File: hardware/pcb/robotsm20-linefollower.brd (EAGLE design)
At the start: 230 x 100 mm, 139 parts, among them Q5 BSS138LT3G, Q6 BSS138LT3G, Q7 BSS138LT3G, Q8 BSS138LT3G, SW1 CTS_219-4LPST, U1 STM32F405RG

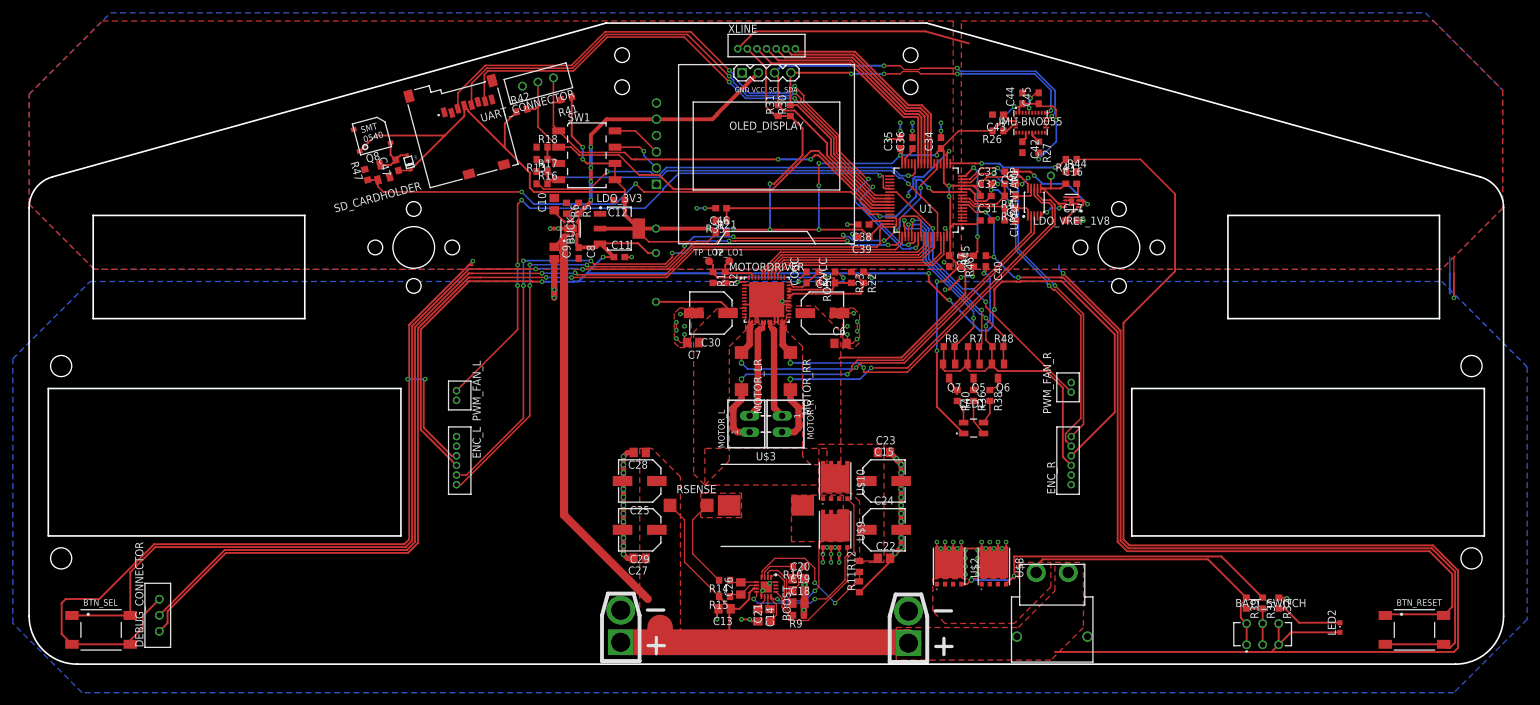
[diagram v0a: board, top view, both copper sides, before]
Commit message: Added more text and continue the DRC fun
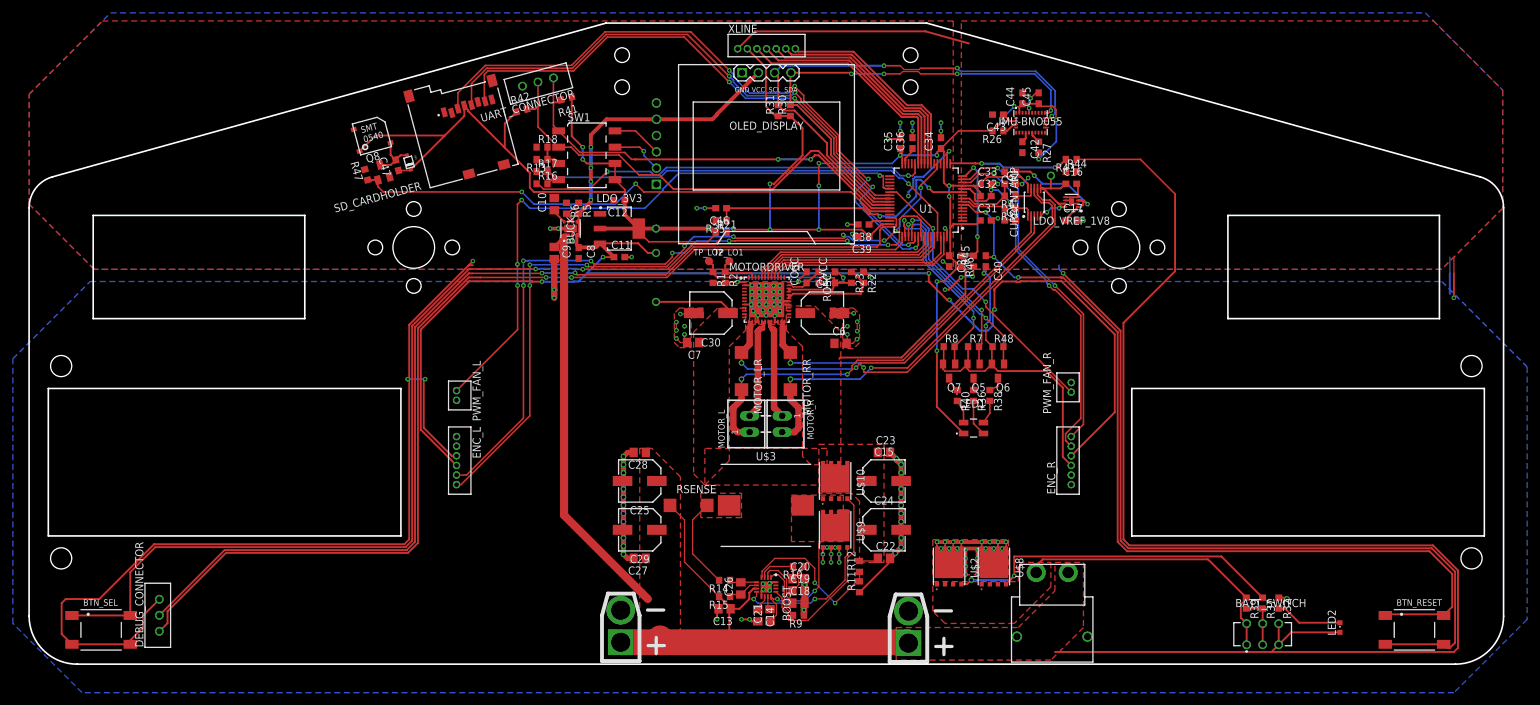
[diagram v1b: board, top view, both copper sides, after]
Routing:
- net GND: track 173.3 -> 251.4 mm, vias 82 -> 110
- net V+: track 406.9 -> 404.8 mm
- net +3V3: track 359.2 -> 357.7 mm
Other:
- board text added: "-"
- board text added: "-->"
- board text added: "."
- board text added: "<--"
- board text added: "RX"
- board text added: "TX"
- board text added: "X"
- board text added: "Y"

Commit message: Check round complete
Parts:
- R32: value 300 -> 300R
- R37: value 100 -> 100R
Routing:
- net BUZZER: track 86.7 -> 85.7 mm
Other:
- board text added: "B0_ON"
- board text added: "B1_ON"
- board text added: "BT_RX"
- board text added: "BT_TX"
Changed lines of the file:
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@@
 <drawing>
 <settings>
-<setting alwaysvectorfont="no"/>
+<setting alwaysvectorfont="yes"/>
 <setting verticaltext="up"/>
 </settings>
@@
 <wire x1="172" y1="20" x2="172" y2="43" width="0.254" layer="20"/>
 <wire x1="172" y1="43" x2="227" y2="43" width="0.254" layer="20"/>
-<text x="212.725" y="9.525" size="1.778" layer="125" ratio="15">RESET</text>
-<text x="8.255" y="9.525" size="1.778" layer="125" ratio="15">SELECT</text>
-<text x="22.86" y="4.445" size="1.016" layer="125" ratio="15">SWCLK</text>
-<text x="22.86" y="6.985" size="1.016" layer="125" ratio="15">SWDIO</text>
-<text x="22.86" y="9.525" size="1.016" layer="125" ratio="15">GND</text>
+<text x="212.725" y="9.525" size="1.778" layer="21" font="vector" ratio="15">RESET</text>
+<text x="7.3406" y="9.906" size="1.778" layer="21" font="vector" ratio="15">SELECT</text>
+<text x="22.9362" y="4.5212" size="1.016" layer="21" font="vector" ratio="15">SWCLK</text>
+<text x="22.9362" y="7.0612" size="1.016" layer="21" font="vector" ratio="15">SWDIO</text>
+<text x="22.9362" y="9.6012" size="1.016" layer="21" font="vector" ratio="15">GND</text>
 <text x="69.215" y="27.94" size="1.016" layer="125" ratio="15">ENC-A</text>
 <text x="69.215" y="29.21" size="1.016" layer="125" ratio="15">ENC-B</text>
@@
 <text x="69.215" y="40.64" size="1.016" layer="125" ratio="15">PWM</text>
 <text x="69.215" y="41.91" size="1.016" layer="125" ratio="15">GND</text>
-<text x="198.12" y="3.175" size="1.27" layer="125" ratio="15">ON</text>
-<text x="183.515" y="3.175" size="1.27" layer="125" ratio="15">OFF</text>
+<text x="198.3486" y="3.7846" size="1.778" layer="21" font="vector" ratio="15">ON</text>
+<text x="183.134" y="3.7846" size="1.778" layer="21" font="vector" ratio="15">OFF</text>
 <text x="96.52" y="54.61" size="1.016" layer="125" ratio="15">12V</text>
 <text x="96.52" y="62.23" size="1.016" layer="125" ratio="15">5V</text>
 <text x="96.52" y="66.04" size="1.016" layer="125" ratio="15">3V3</text>
 <text x="158.3944" y="74.2696" size="1.016" layer="125" ratio="15">1V8</text>
-<text x="108.585" y="95.25" size="1.016" layer="125" ratio="15" rot="R90">GND</text>
-<text x="122.555" y="94.615" size="1.016" layer="125" ratio="15" rot="R90">MUX3</text>
+<text x="108.585" y="95.25" size="1.016" layer="21" font="vector" ratio="15" rot="R90">GND</text>
+<text x="122.555" y="94.615" size="1.016" layer="21" font="vector" ratio="15" rot="R90">MUX3</text>
 <text x="155.575" y="17.145" size="1.016" layer="125" ratio="15">BAT-</text>
 <text x="161.29" y="17.145" size="1.016" layer="125" ratio="15">V+</text>
@@
 <rectangle x1="80.9625" y1="54.2163" x2="82.9437" y2="54.2925" layer="201"/>
 <rectangle x1="81.4197" y1="54.2925" x2="82.9437" y2="54.3687" layer="201"/>
-<text x="85.1916" y="34.1376" size="1.016" layer="125" ratio="15" align="top-center">Blitz V2
+<text x="85.1916" y="34.1376" size="1.016" layer="125" font="vector" ratio="18" align="top-center">Blitz V2
 rev 1.0
 2020-03-13
@@
 Board 19/02
 </text>
-<text x="11.811" y="75.2602" size="1.016" layer="125" ratio="15" rot="R15">https://github.com/caselabbet/robotsm20-linefollower</text>
+<text x="11.811" y="75.2602" size="1.016" layer="125" font="vector" ratio="15" rot="R15">https://github.com/caselabbet/robotsm20-linefollower</text>
 <text x="162.941" y="86.2584" size="1.016" layer="125" ratio="15">X</text>
 <text x="163.83" y="87.3506" size="1.016" layer="125" ratio="15" rot="R90">--&gt;</text>
@@
 <text x="101.8286" y="57.2262" size="1.9304" layer="125" ratio="15" distance="104">-</text>
 <text x="144.3482" y="35.814" size="1.9304" layer="125" ratio="15" distance="104">.</text>
-<text x="73.8632" y="91.3892" size="1.016" layer="125" ratio="15" rot="R15">GND</text>
-<text x="77.8256" y="92.456" size="1.016" layer="125" ratio="15" rot="R15">TX</text>
-<text x="80.3402" y="93.1418" size="1.016" layer="125" ratio="15" rot="R15">RX</text>
+<text x="73.8632" y="91.3892" size="1.016" layer="21" font="vector" ratio="15" rot="R15">GND</text>
+<text x="77.8256" y="92.456" size="1.016" layer="21" font="vector" ratio="15" rot="R15">TX</text>
+<text x="80.3402" y="93.1418" size="1.016" layer="21" font="vector" ratio="15" rot="R15">RX</text>
+<text x="92.9132" y="82.7786" size="1.016" layer="21" font="vector" ratio="15">BT_RX</text>
+<text x="93.0656" y="80.1878" size="1.016" layer="21" font="vector" ratio="15">BT_TX</text>
+<text x="92.9132" y="77.5208" size="1.016" layer="21" font="vector" ratio="15">B0_ON</text>
+<text x="92.837" y="75.1586" size="1.016" layer="21" font="vector" ratio="15">B1_ON</text>
 </plain>
 <attributes>
@@
 <attribute name="VALUE" x="192.42" y="4.453" size="1.27" layer="27" align="center"/>
 </element>
-<element name="R37" library="rcl" library_urn="urn:adsk.eagle:library:334" package="R0603" package3d_urn="urn:adsk.eagle:package:23555/3" value="100" x="192.405" y="9.525" smashed="yes" rot="R270">
+<element name="R37" library="rcl" library_urn="urn:adsk.eagle:library:334" package="R0603" package3d_urn="urn:adsk.eagle:package:23555/3" value="100R" x="192.405" y="9.525" smashed="yes" rot="R270">
 <attribute name="NAME" x="193.04" y="10.16" size="1.27" layer="25" rot="R270"/>
 <attribute name="POPULARITY" value="70" x="192.405" y="9.525" size="1.778" layer="27" rot="R270" display="off"/>
@@
 <attribute name="VALUE" x="190.5" y="10.16" size="1.27" layer="27" rot="R270"/>
 </element>
-<element name="R32" library="rcl" library_urn="urn:adsk.eagle:library:334" package="R0603" package3d_urn="urn:adsk.eagle:package:23555/3" value="300" x="194.945" y="9.525" smashed="yes" rot="R270">
+<element name="R32" library="rcl" library_urn="urn:adsk.eagle:library:334" package="R0603" package3d_urn="urn:adsk.eagle:package:23555/3" value="300R" x="194.945" y="9.525" smashed="yes" rot="R270">
 <attribute name="NAME" x="195.58" y="10.16" size="1.27" layer="25" rot="R270"/>
 <attribute name="POPULARITY" value="70" x="194.945" y="9.525" size="1.778" layer="27" rot="R270" display="off"/>
@@
 <wire x1="112.395" y1="6.985" x2="111.125" y2="6.985" width="0.3" layer="1"/>
 <polygon width="0.3" layer="16" thermals="no">
-<vertex x="9.525" y="59.69"/>
+<vertex x="9.6012" y="59.69"/>
 <vertex x="220.345" y="59.69"/>
 <vertex x="233.68" y="46.355"/>
@@
 <vertex x="8.255" y="-4.445"/>
 <vertex x="-2.54" y="6.35"/>
-<vertex x="-2.54" y="47.625"/>
+<vertex x="-2.54" y="47.5488"/>
 </polygon>
 <via x="92.71" y="22.225" extent="1-16" drill="0.5"/>
@@
 <wire x1="54.39833125" y1="75.530425" x2="54.41206875" y2="75.516603125" width="0.3048" layer="1"/>
 <wire x1="130.1518375" y1="71.7318375" x2="128.223675" y2="73.66" width="0.254" layer="1"/>
-<wire x1="128.223675" y1="73.66" x2="95.885" y2="73.66" width="0.254" layer="1"/>
-<wire x1="95.885" y1="73.66" x2="94.615" y2="74.93" width="0.254" layer="1"/>
-<via x="94.615" y="74.93" extent="1-16" drill="0.35"/>
-<wire x1="94.615" y1="74.93" x2="91.44" y2="71.755" width="0.254" layer="16"/>
-<wire x1="91.44" y1="71.755" x2="78.74" y2="71.755" width="0.254" layer="16"/>
+<wire x1="128.223675" y1="73.66" x2="96.2406" y2="73.66" width="0.254" layer="1"/>
+<wire x1="96.2406" y1="73.66" x2="95.377" y2="72.7964" width="0.254" layer="1"/>
+<via x="95.377" y="72.7964" extent="1-16" drill="0.35"/>
+<wire x1="95.377" y1="72.7964" x2="94.3356" y2="71.755" width="0.254" layer="16"/>
+<wire x1="94.3356" y1="71.755" x2="78.74" y2="71.755" width="0.254" layer="16"/>
 <wire x1="78.74" y1="71.755" x2="76.835" y2="73.66" width="0.254" layer="16"/>
 <via x="76.835" y="73.66" extent="1-16" drill="0.35"/>
@@
 <contactref element="BT_HC05" pad="2"/>
 <contactref element="SW1" pad="A2"/>
-<wire x1="97.86" y1="77.373" x2="95.885" y2="79.348" width="0.254" layer="16"/>
-<wire x1="95.885" y1="79.348" x2="95.885" y2="80.01" width="0.254" layer="16"/>
-<via x="95.885" y="80.01" extent="1-16" drill="0.35"/>
-<wire x1="95.885" y1="80.01" x2="95.25" y2="80.645" width="0.254" layer="1"/>
+<wire x1="97.86" y1="77.373" x2="96.4184" y2="78.8146" width="0.254" layer="16"/>
+<wire x1="96.4184" y1="79.4766" x2="96.4184" y2="78.8146" width="0.254" layer="16"/>
+<via x="96.4184" y="79.4766" extent="1-16" drill="0.35"/>
+<wire x1="96.4184" y1="79.4766" x2="95.25" y2="80.645" width="0.254" layer="1"/>
 <wire x1="95.25" y1="80.645" x2="91.395" y2="80.645" width="0.254" layer="1"/>
 </signal>

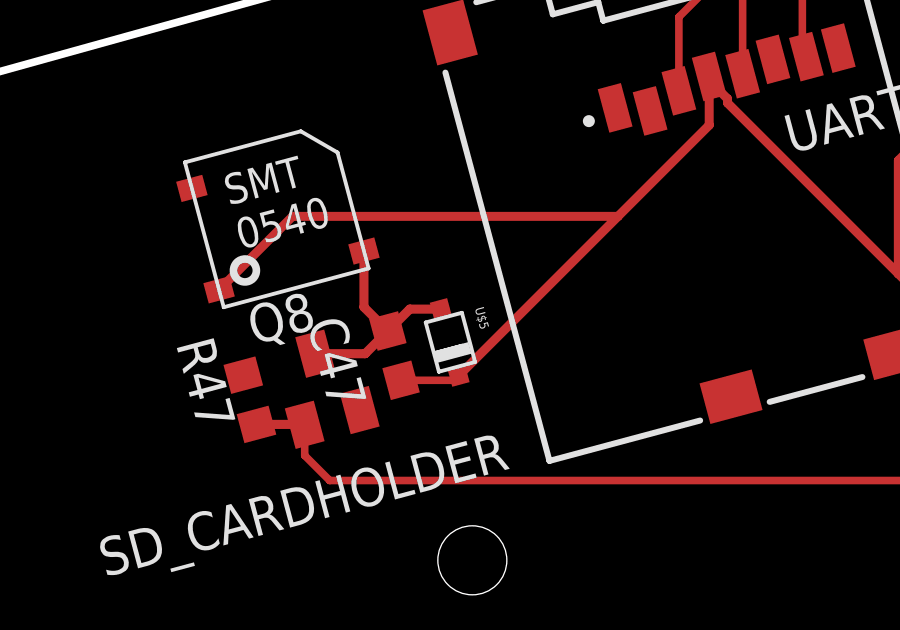
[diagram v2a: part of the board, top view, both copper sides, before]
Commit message: Removed unused pins
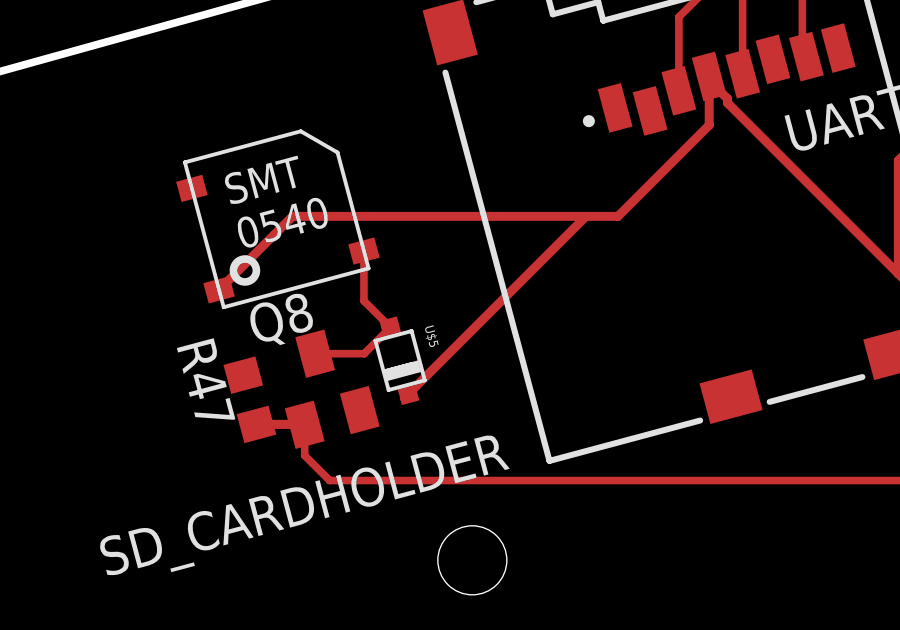
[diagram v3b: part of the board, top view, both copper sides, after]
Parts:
- removed C47: (no value), rcl:C0603
- moved U$5 1.78 mm to (57.5, 77.9)
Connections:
- net MISO renamed N$6
- net MOSI renamed N$5
- net SCK renamed N$9
- net +3V3: no longer C47.1
- net AGND: no longer IMU-BNO055.10
- net N$33: no longer C47.2
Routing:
- net N$33: track 7.80 -> 5.79 mm
- net +3V3: track 357.7 -> 356.8 mm

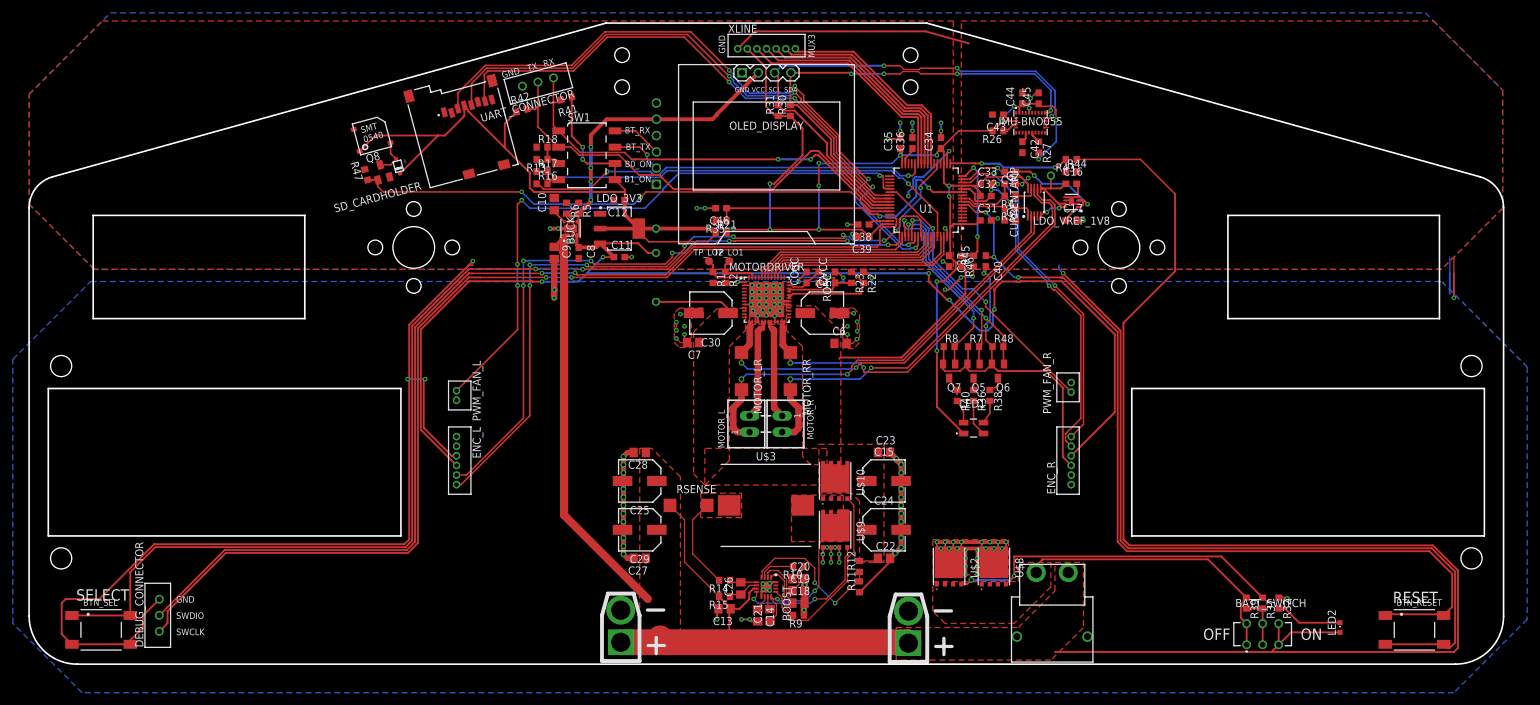
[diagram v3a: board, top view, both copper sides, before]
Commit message: DRC and ERC check complete
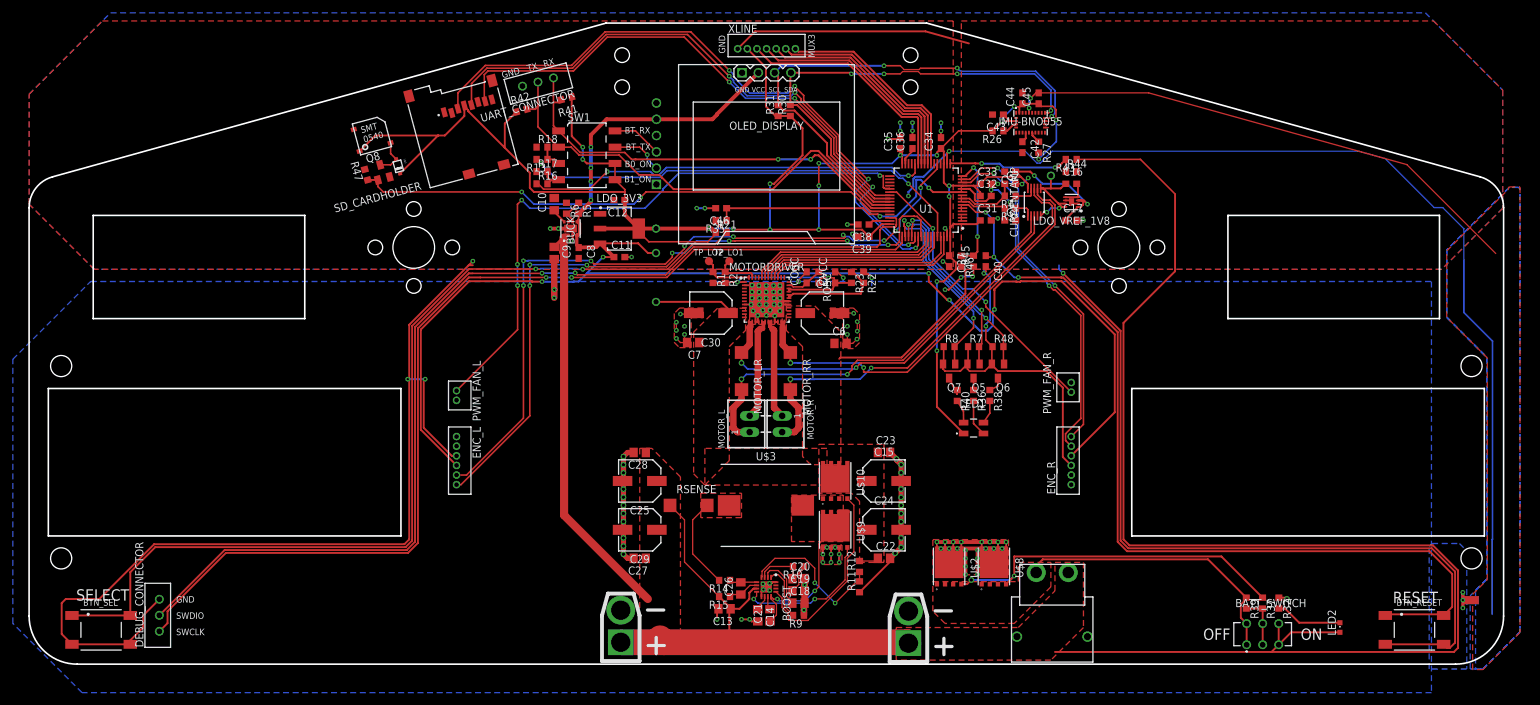
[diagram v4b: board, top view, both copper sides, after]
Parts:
- U$4, U$6: device Isaks Bibliotek:SPLITTER -> PowerManagement:SPLITTER
- moved U$4 51.1 mm to (224.9, 9.98), flipped to the top, turned to 270 degrees
- moved U$6 51.0 mm to (224.9, 9.98), flipped to the bottom, turned to 90 degrees
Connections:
- removed net IMU_INT: IMU-BNO055.14
- net AGND: now also U$4.P$1; no longer U$6.1
- net DGND: now also U$6.P$1; no longer U$4.1
- net GND: now also U$4.P$2, U$6.P$2; no longer U$4.2, U$6.2
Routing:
- net DGND: track 373.7 -> 519.7 mm
- net AGND: track 67.8 -> 143.8 mm
- net GND: track 251.4 -> 248.7 mm, vias 110 -> 112
